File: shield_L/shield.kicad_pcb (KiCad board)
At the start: 2 copper layers, 85.1 x 78.7 mm, 15 parts, among them J3 Conn_01x01, J4 Conn_01x01, J5 Conn_01x01

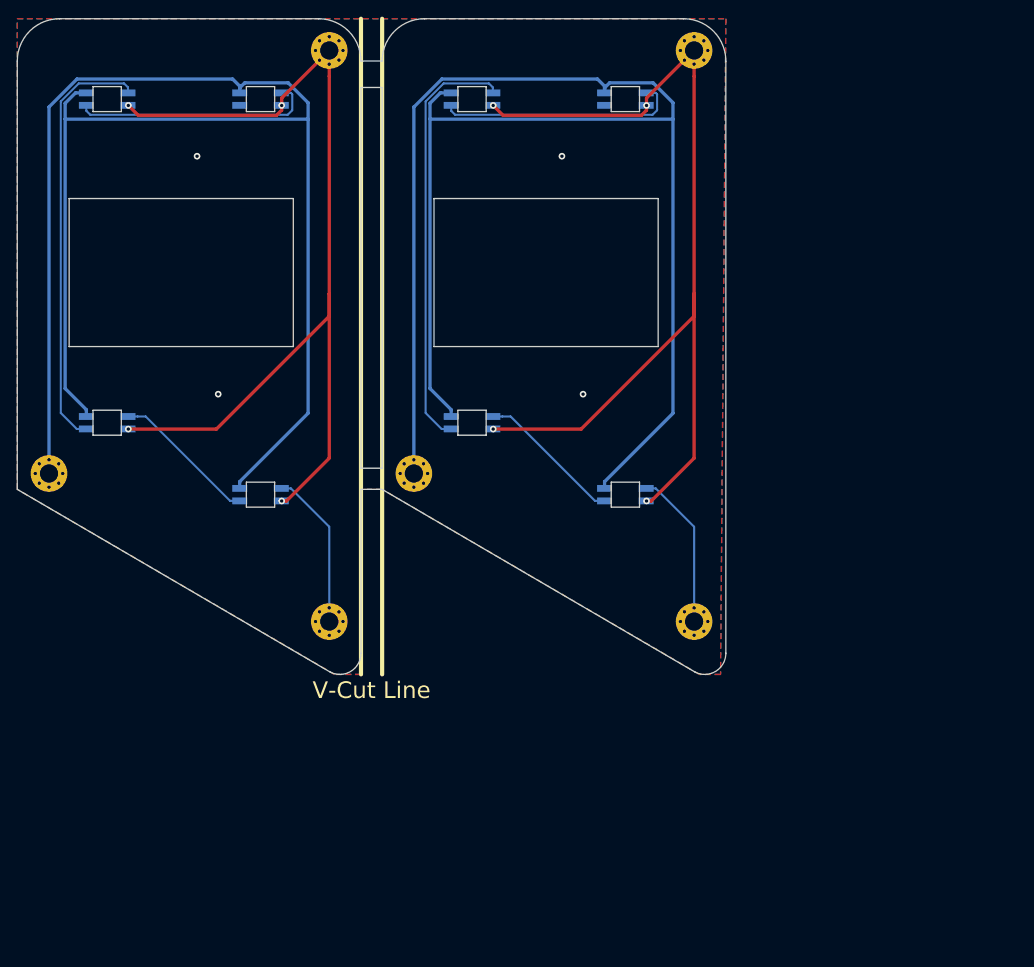
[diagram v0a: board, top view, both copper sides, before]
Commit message: change shelds v-cut
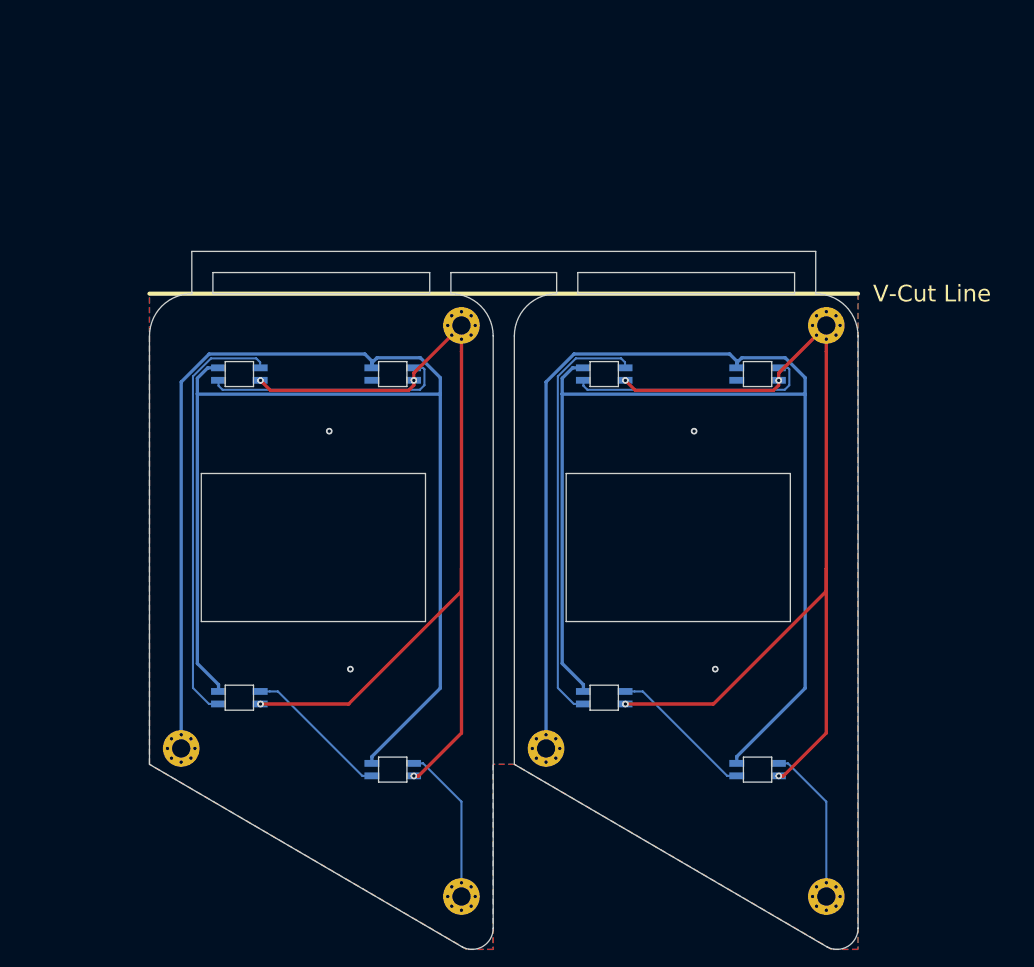
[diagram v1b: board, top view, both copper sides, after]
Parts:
- moved L1 36.6 mm to (104.1, 102.9)
- moved L1 36.6 mm to (60.3, 102.9)
- moved J3 36.6 mm to (112.4, 118.1)
- moved J3 36.6 mm to (68.6, 118.1)
- moved J4 36.6 mm to (78.7, 100.3)
- moved J4 36.6 mm to (34.9, 100.3)
- moved J5 36.6 mm to (112.4, 49.5)
- moved J5 36.6 mm to (68.6, 49.5)
- moved L2 36.6 mm to (85.7, 94.2)
- moved L2 36.6 mm to (41.9, 94.2)
- moved L3 36.6 mm to (85.7, 55.4)
- moved L3 36.6 mm to (41.9, 55.4)
- moved L4 36.6 mm to (104.1, 55.4)
- moved L4 36.6 mm to (60.3, 55.4)
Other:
- board size 85.1 x 78.7 mm -> 85.1 x 83.8 mm
